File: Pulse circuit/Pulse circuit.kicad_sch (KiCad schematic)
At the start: 9 parts, among them U1 module_max30102, U2 module_max30102, U3 DOIT-ESP32-DEVKIT-V1

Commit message: Changed footprint of the resistors
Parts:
- R10, R7, R8, R9: footprint Resistor_THT:R_Axial_DIN0204_L3.6mm_D1.6mm_P5.08mm_Horizontal -> Resistor_THT:R_Axial_DIN0207_L6.3mm_D2.5mm_P7.62mm_Horizontal
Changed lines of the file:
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@@
 			)
 		)
-		(property "Footprint" "Resistor_THT:R_Axial_DIN0204_L3.6mm_D1.6mm_P5.08mm_Horizontal"
+		(property "Footprint" "Resistor_THT:R_Axial_DIN0207_L6.3mm_D2.5mm_P7.62mm_Horizontal"
 			(at 64.262 72.39 90)
 			(effects
@@
 			)
 		)
-		(property "Footprint" "Resistor_THT:R_Axial_DIN0204_L3.6mm_D1.6mm_P5.08mm_Horizontal"
+		(property "Footprint" "Resistor_THT:R_Axial_DIN0207_L6.3mm_D2.5mm_P7.62mm_Horizontal"
 			(at 96.012 73.66 90)
 			(effects
@@
 			)
 		)
-		(property "Footprint" "Resistor_THT:R_Axial_DIN0204_L3.6mm_D1.6mm_P5.08mm_Horizontal"
+		(property "Footprint" "Resistor_THT:R_Axial_DIN0207_L6.3mm_D2.5mm_P7.62mm_Horizontal"
 			(at 93.472 73.66 90)
 			(effects
@@
 			)
 		)
-		(property "Footprint" "Resistor_THT:R_Axial_DIN0204_L3.6mm_D1.6mm_P5.08mm_Horizontal"
+		(property "Footprint" "Resistor_THT:R_Axial_DIN0207_L6.3mm_D2.5mm_P7.62mm_Horizontal"
 			(at 66.802 72.39 90)
 			(effects

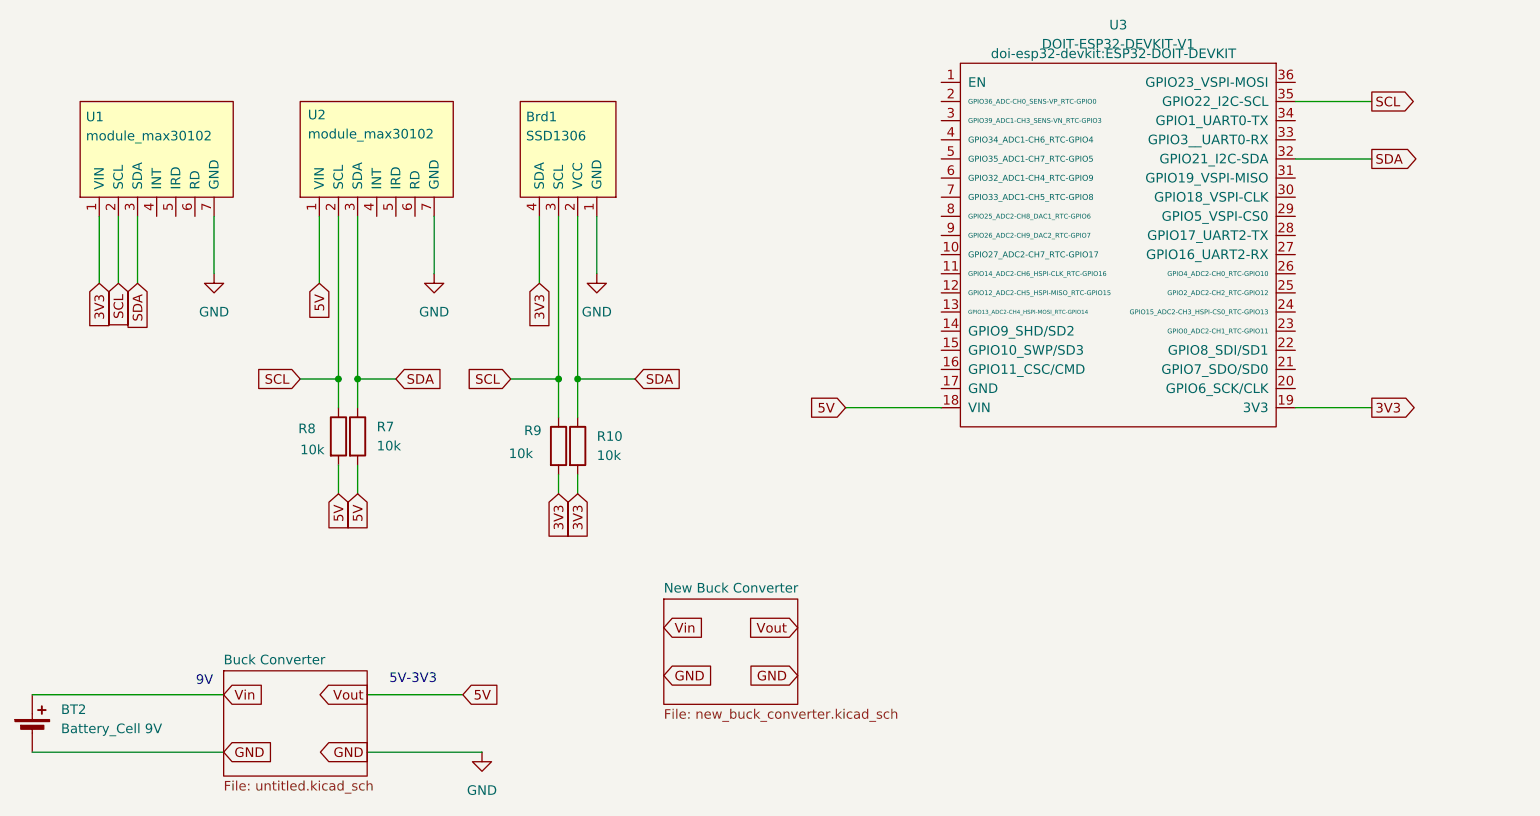
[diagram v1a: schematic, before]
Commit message: Added a button
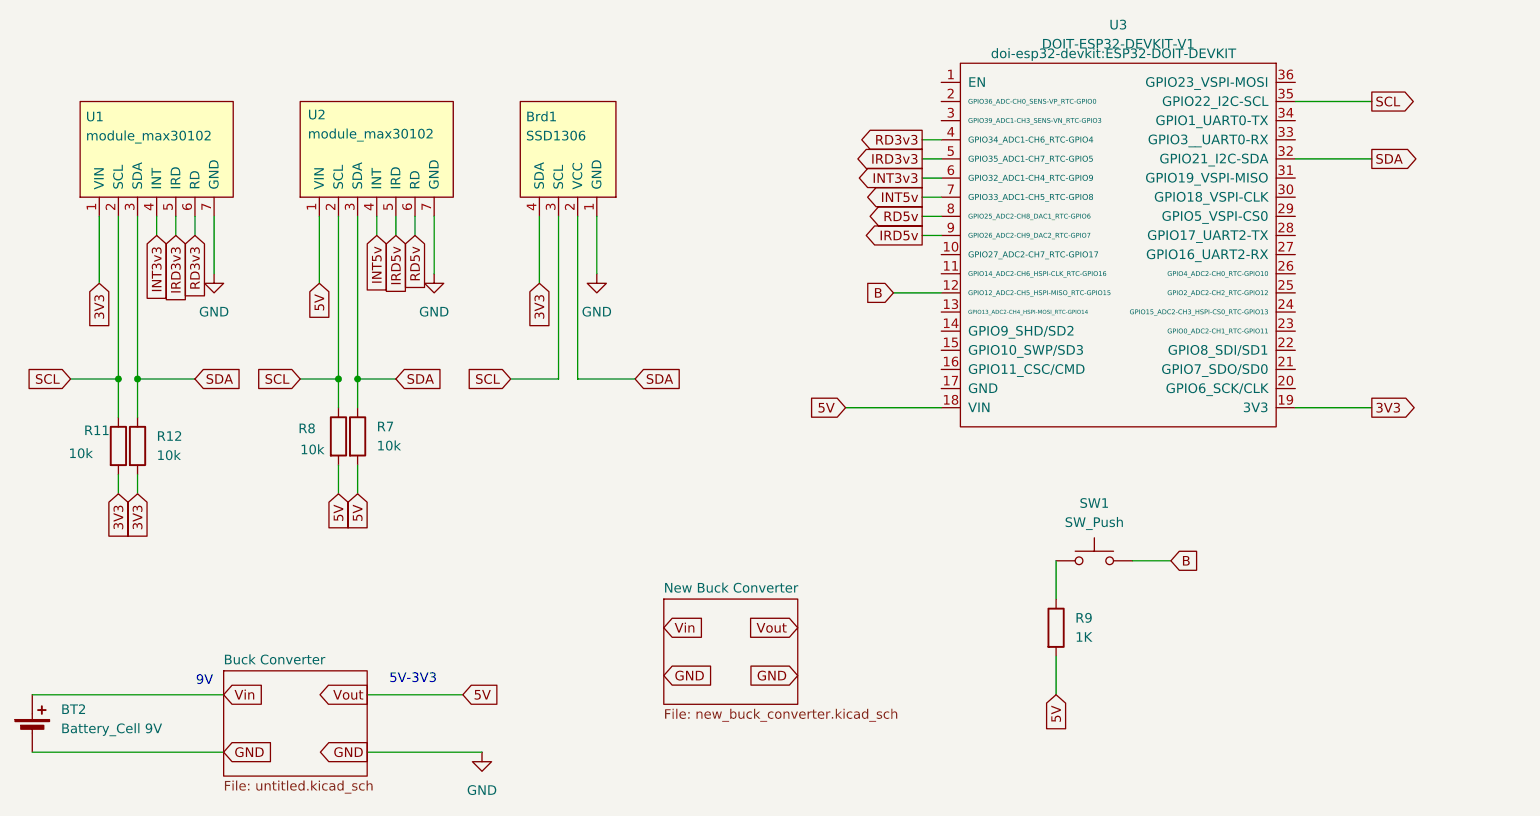
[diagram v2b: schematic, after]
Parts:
- removed R10: 10k, Resistor_THT:R_Axial_DIN0207_L6.3mm_D2.5mm_P7.62mm_Horizontal, symbol Device:R
- added R11, R12: 10k, Resistor_THT:R_Axial_DIN0207_L6.3mm_D2.5mm_P7.62mm_Horizontal, symbol Device:R
- added SW1: SW_Push, symbol Switch:SW_Push
- R9: value 10k -> 1K; footprint Resistor_THT:R_Axial_DIN0207_L6.3mm_D2.5mm_P7.62mm_Horizontal -> (none)
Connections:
- net 3V3: now also R11.2, R12.2; no longer R9.2
- net 5V: now also R9.2
- net SCL: now also R11.1; no longer R9.1
- net SDA: now also R12.1
- net INT3v3: now reaches U1.4 (INT)
- net INT3v3: now also U3.6 (GPIO32_ADC1-CH4_RTC-GPIO9)
- net IRD3v3: now reaches U1.5 (IRD)
- net IRD3v3: now also U3.5 (GPIO35_ADC1-CH7_RTC-GPIO5)
- net RD3v3: now reaches U1.6 (RD)
- net RD3v3: now also U3.4 (GPIO34_ADC1-CH6_RTC-GPIO4)
- net INT5v: now reaches U2.4 (INT)
- net INT5v: now also U3.7 (GPIO33_ADC1-CH5_RTC-GPIO8)
- net IRD5v: now reaches U2.5 (IRD)
- net IRD5v: now also U3.9 (GPIO26_ADC2-CH9_DAC2_RTC-GPIO7)
- net RD5v: now reaches U2.6 (RD)
- net RD5v: now also U3.8 (GPIO25_ADC2-CH8_DAC1_RTC-GPIO6)
- net B: now reaches U3.12 (GPIO12_ADC2-CH5_HSPI-MISO_RTC-GPIO15)
- net B: now also SW1.2
- new net: R9.1, SW1.1

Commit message: Rerouted the PCB
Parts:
- added J1: Conn_01x02_Pin, Connector_Wire:SolderWire-1.5sqmm_1x02_P6mm_D1.7mm_OD3mm, symbol Connector:Conn_01x02_Pin
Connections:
- net 5V: now also J1.2 (Pin_2)
- net GND: now also U3.17 (GND), J1.1 (Pin_1)

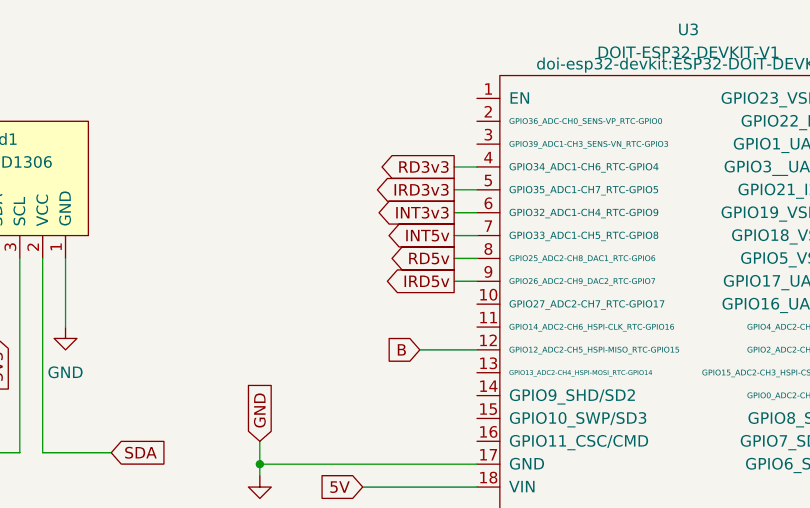
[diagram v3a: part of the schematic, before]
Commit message: Final design
Need to double check size of esp32
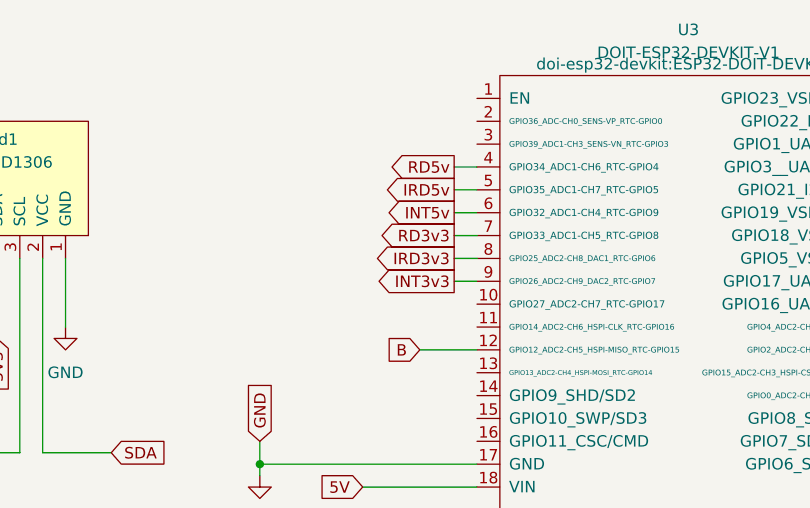
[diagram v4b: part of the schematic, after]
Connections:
- net INT3v3: now also U3.9 (GPIO26_ADC2-CH9_DAC2_RTC-GPIO7); no longer U3.6 (GPIO32_ADC1-CH4_RTC-GPIO9)
- net INT5v: now also U3.6 (GPIO32_ADC1-CH4_RTC-GPIO9); no longer U3.7 (GPIO33_ADC1-CH5_RTC-GPIO8)
- net IRD3v3: now also U3.8 (GPIO25_ADC2-CH8_DAC1_RTC-GPIO6); no longer U3.5 (GPIO35_ADC1-CH7_RTC-GPIO5)
- net IRD5v: now also U3.5 (GPIO35_ADC1-CH7_RTC-GPIO5); no longer U3.9 (GPIO26_ADC2-CH9_DAC2_RTC-GPIO7)
- net RD3v3: now also U3.7 (GPIO33_ADC1-CH5_RTC-GPIO8); no longer U3.4 (GPIO34_ADC1-CH6_RTC-GPIO4)
- net RD5v: now also U3.4 (GPIO34_ADC1-CH6_RTC-GPIO4); no longer U3.8 (GPIO25_ADC2-CH8_DAC1_RTC-GPIO6)
